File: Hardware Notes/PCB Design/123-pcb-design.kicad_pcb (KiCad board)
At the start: 2 copper layers, 20 parts, among them J1 JST 1x02, J2 JST 1x02, J3 JST 1x04, U1 ESP32-C3-MINI-1, U2 MCP73871, U3 HX711

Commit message: pcb rev 4 w/ battery monitor circuit
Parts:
- added R6: 1K, Resistor_SMD:R_0402_1005Metric, F.Cu at (143.5, 63.5)
- added R7: 1K, Resistor_SMD:R_0402_1005Metric, F.Cu at (144.5, 65.5)
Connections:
- U1 pad 5: unconnected-(U1-GPIO2/ADC1_CH2-Pad5) -> Net-(U1-GPIO2/ADC1_CH2)
- U2 pad 10: GND -> Net-(U2-V_{SS}-Pad10)
- U2 pad 11: GND -> Net-(U2-V_{SS}-Pad10)
- U2 pad 14: Net-(U2-V_{BAT}-Pad14) -> Net-(J2-Pin_1)
- U2 pad 15: U2-V_{BAT}-Pad15 -> Net-(J2-Pin_1)
- U2 pad 16: Net-(U2-V_{BAT_SENSE}) -> Net-(J2-Pin_1)
- U2 pad 18: U2-J1_POS -> Net-(J1-Pin_1)
- U2 pad 21: GND -> Net-(U2-V_{SS}-Pad10)
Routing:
- net Net-(U1-GPIO2/ADC1_CH2): track 0.00 -> 3.07 mm
- net VSUP: track 25.2 -> 27.7 mm
- net U2-J1_POS: vias 1 -> 0
- net Net-(J1-Pin_1): vias 0 -> 1

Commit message: removed resistor from voltage supply path
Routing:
- net VSUP: track 27.7 -> 38.4 mm
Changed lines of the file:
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@@
 	)
 	(segment
-		(start 139.8125 73.125)
-		(end 142.1 73.125)
+		(start 142.99 71.765)
+		(end 143.225 72)
 		(width 0.2)
 		(layer "F.Cu")
@@
 	)
 	(segment
-		(start 143.225 63.735)
-		(end 142.99 63.5)
+		(start 142.99 63.5)
+		(end 142.99 71.765)
 		(width 0.2)
 		(layer "F.Cu")
@@
 	)
 	(segment
-		(start 145.69 60.8)
-		(end 146.625 60.8)
+		(start 139.8125 73.125)
+		(end 142.1 73.125)
 		(width 0.2)
 		(layer "F.Cu")
@@
 	)
 	(segment
+		(start 144.2 60.8)
+		(end 142 63)
+		(width 0.2)
+		(layer "F.Cu")
+		(net "VSUP")
+	)
+	(segment
+		(start 142.5 72)
+		(end 143.225 72)
+		(width 0.2)
+		(layer "F.Cu")
+		(net "VSUP")
+	)
+	(segment
 		(start 142.1 73.125)
 		(end 143.225 72)
@@
 	)
 	(segment
-		(start 143.225 72)
-		(end 143.225 63.735)
+		(start 146.625 60.8)
+		(end 144.2 60.8)
 		(width 0.2)
 		(layer "F.Cu")
@@
 	)
 	(segment
+		(start 142 71.5)
+		(end 142.5 72)
+		(width 0.2)
+		(layer "F.Cu")
+		(net "VSUP")
+	)
+	(segment
 		(start 144.45 73.225)
 		(end 145.321196 73.225)
+		(width 0.2)
+		(layer "F.Cu")
+		(net "VSUP")
+	)
+	(segment
+		(start 142 63)
+		(end 142 71.5)
 		(width 0.2)
 		(layer "F.Cu")
@@
 		(width 0.2)
 		(layer "F.Cu")
-		(net "VSUP")
-	)
-	(segment
-		(start 142.99 63.5)
-		(end 145.69 60.8)
-		(width 0.2)
-		(layer "F.Cu")

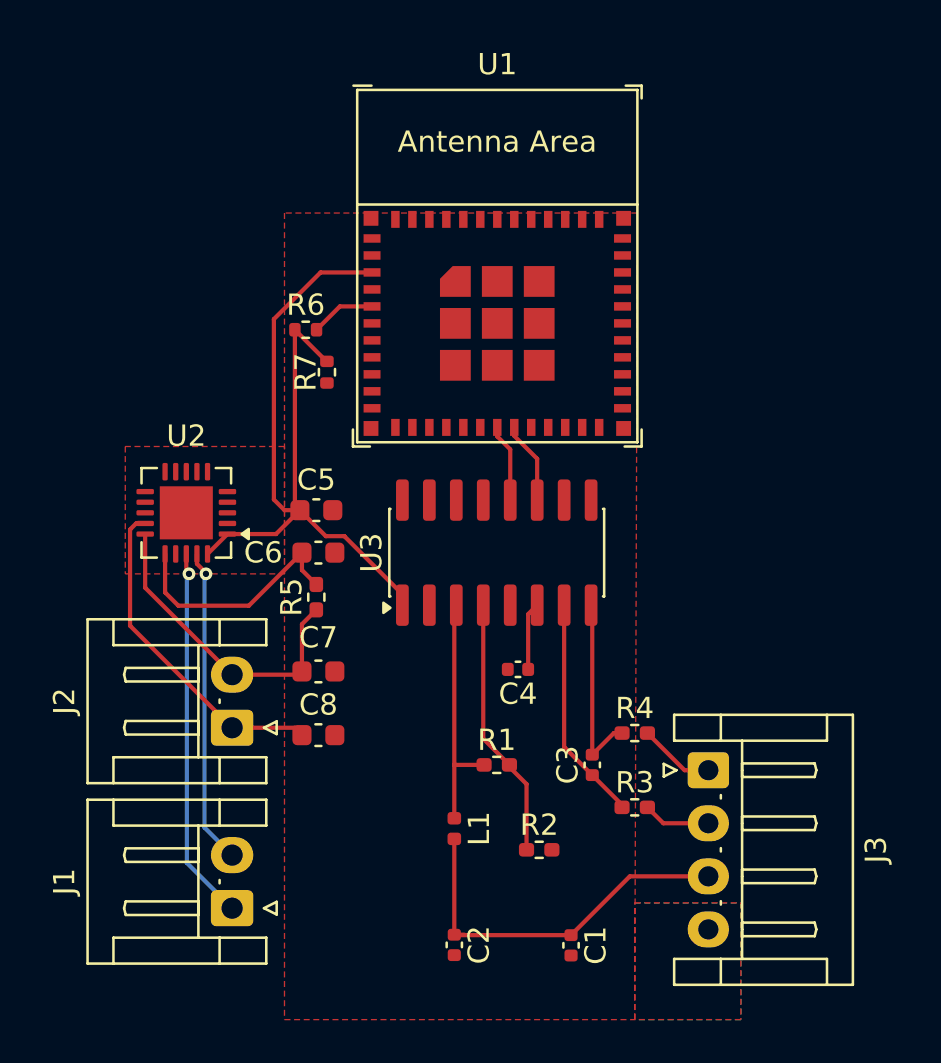
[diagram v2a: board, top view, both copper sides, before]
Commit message: DRC passes for schematic
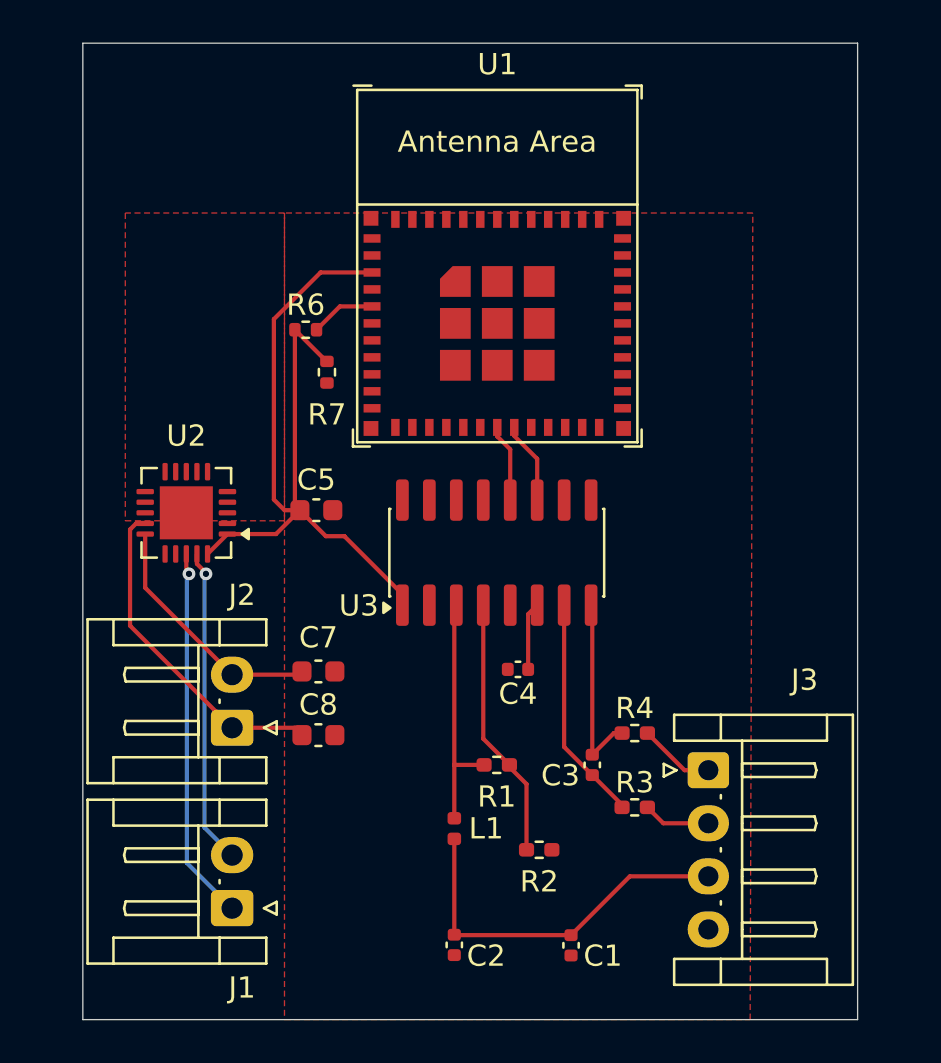
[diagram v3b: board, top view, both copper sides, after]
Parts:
- removed C6: 4.7μF, Capacitor_SMD:C_0603_1608Metric
- removed R5: 0, Resistor_SMD:R_0402_1005Metric_Pad0.72x0.64mm_HandSolder
- R6: value 1K -> 100k
- R7: value 1K -> 100K
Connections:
- C1 pad 1: Net-(U3-AVDD) -> J3_Pin_3
- C2 pad 1: Net-(U3-AVDD) -> J3_Pin_3
- J3 pad 1: Net-(U3-INA+) -> J3_Pin_1
- J3 pad 2: Net-(U3-INA-) -> J3_Pin_2
- J3 pad 3: Net-(U3-AVDD) -> J3_Pin_3
- L1 pad 2: Net-(U3-AVDD) -> J3_Pin_3
- R3 pad 2: Net-(U3-INA-) -> J3_Pin_2
- R4 pad 2: Net-(U3-INA+) -> J3_Pin_1
- U2 pad 10: Net-(U2-V_{SS}-Pad10) -> GND
- U2 pad 11: Net-(U2-V_{SS}-Pad10) -> GND
- U2 pad 14: Net-(J2-Pin_1) -> Net-(U2-V_{BAT}-Pad14)
- U2 pad 15: Net-(J2-Pin_1) -> U2-V_{BAT}-Pad15
- U2 pad 16: Net-(J2-Pin_1) -> (no net)
- U2 pad 18: Net-(J1-Pin_1) -> U2-J1_POS
- U2 pad 21: Net-(U2-V_{SS}-Pad10) -> GND
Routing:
- net Net-(U3-AVDD): track 29.8 -> 11.5 mm
- net J3_Pin_3: track 0.00 -> 17.7 mm
- net Net-(U2-V_{BAT_SENSE}): track 11.3 -> 0.00 mm
- net J3_Pin_1: track 0.00 -> 3.59 mm
- net Net-(U3-INA+): track 12.5 -> 8.89 mm
- net U2-V_{BAT}-Pad15: track 14.9 -> 11.7 mm
- net J3_Pin_2: track 0.00 -> 3.18 mm
- net Net-(U3-INA-): track 13.8 -> 10.7 mm
- net U2-J1_POS: track 17.6 -> 17.7 mm, vias 0 -> 1
- net Net-(J1-Pin_1): vias 1 -> 0
- removed copper zone on B.Cu, net GND
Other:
- board outline added: 36.5 x 46 mm

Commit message: new pcb documents, references added to schematic
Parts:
- added C8: 10μF, Capacitor_SMD:C_0603_1608Metric, F.Cu at (144.5, 88.0)
- added C9: 10μF, Capacitor_SMD:C_0603_1608Metric, F.Cu at (144.5, 91.0)
- renumbered C7 to C6, C8 to C7, R6 to R5, R7 to R6
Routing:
- net U2-J1_NEG: track 14.9 -> 19.8 mm
- net U2-J1_POS: track 17.7 -> 21.5 mm
- net U2-V_{BAT}-Pad15: track 11.7 -> 13.0 mm
